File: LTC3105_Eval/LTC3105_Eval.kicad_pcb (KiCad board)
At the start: 2 copper layers, 29.1 x 15.2 mm, 14 parts, among them J1 Conn_01x05_Pin, J2 Conn_01x05_Pin, U1 LTC3105EMS

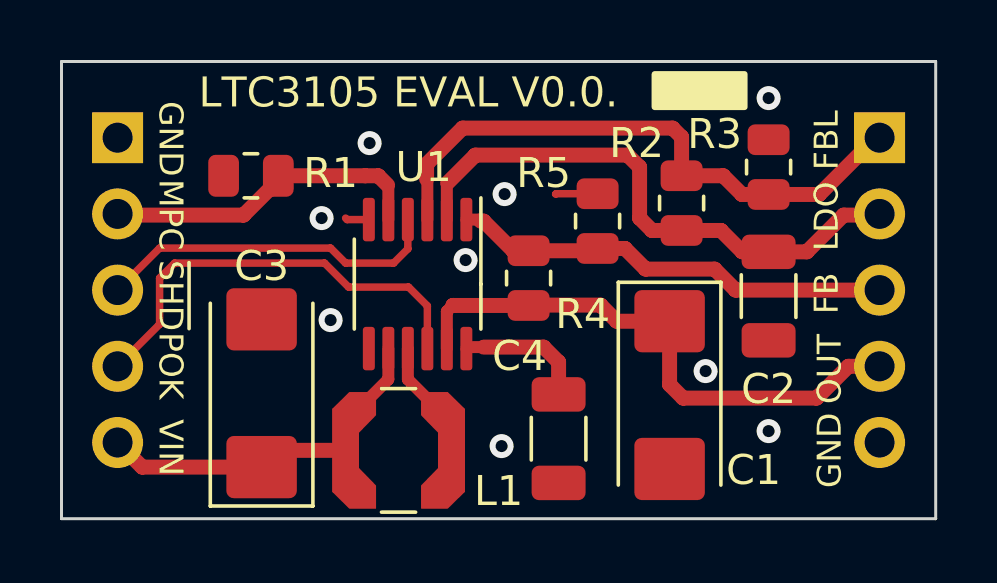
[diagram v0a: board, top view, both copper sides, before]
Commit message: resolved #8, #7, #6 and #5 ; closed #5 and #3
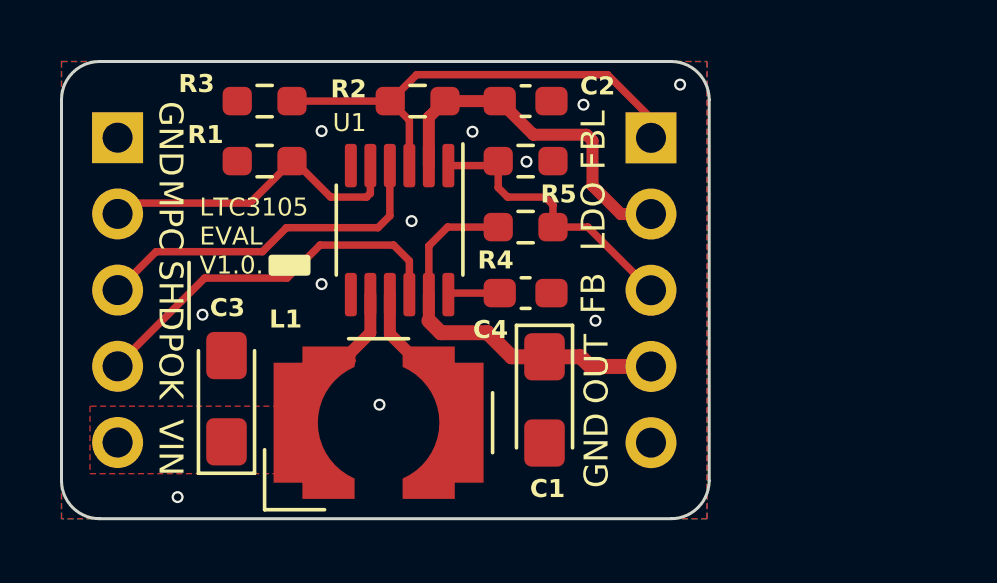
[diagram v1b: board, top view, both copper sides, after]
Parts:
- removed G***: LOGO, QRCODE.preety:LTC3105_Eval_V0_QRCode_5x5
- C1, C3: footprint Capacitor_Tantalum_SMD:CP_EIA-6032-28_Kemet-C -> Capacitor_Tantalum_SMD:CP_EIA-3216-18_Kemet-A_Pad1.58x1.35mm_HandSolder
- C2, C4: footprint Capacitor_SMD:C_1206_3216Metric -> Capacitor_SMD:C_0603_1608Metric_Pad1.08x0.95mm_HandSolder
- L1: value 10uF -> 10uH; footprint Inductor_SMD:L_Coilcraft_LPS4018 -> 021_inductor:L_Coilcraft_MSS5131-XXX_handsolder
- R1, R2, R3, R4, R5: footprint Resistor_SMD:R_0805_2012Metric -> Resistor_SMD:R_0603_1608Metric_Pad0.98x0.95mm_HandSolder
- moved R3 16.9 mm to (131.9, 95.3), turned to 180 degrees
- moved C2 10.4 mm to (140.6, 95.3), turned to 0 degrees
- moved R2 9.43 mm to (137.0, 95.3), turned to 180 degrees
- moved J2 7.62 mm to (144.8, 96.5)
- moved C4 4.98 mm to (140.6, 101.7), turned to 0 degrees
- moved C1 4.17 mm to (141.2, 105.3)
- moved R5 3.12 mm to (140.6, 97.3), turned to 0 degrees
- moved U1 1.90 mm to (136.4, 99.6)
- moved R4 1.70 mm to (140.6, 99.5), turned to 0 degrees
- moved C3 1.18 mm to (130.6, 105.2)
- moved L1 1.14 mm to (135.7, 106.0), turned to 90 degrees
- moved R1 0.67 mm to (131.9, 97.3)
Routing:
- net VIN: track 12.7 -> 2.55 mm
- net LDO_OUT: track 18.9 -> 11.7 mm
- net VOUT: track 18.7 -> 13.1 mm
- net FB: track 14.8 -> 9.55 mm
- net FB_LDO: track 19.9 -> 15.9 mm
- net Net-(U1-AUX): track 4.38 -> 1.73 mm
- net GND: track 2.20 -> 0.00 mm, vias 9 -> 11
- net POWERGOOD: track 14.7 -> 12.8 mm
- net /SW: track 3.99 -> 2.69 mm
- added copper zone on F.Cu, net VIN
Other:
- board size 29.1 x 15.2 mm -> 21.6 x 15.2 mm
- board text added: "LTC3105 EVAL V1.0."
- board text removed: "LTC3105 EVAL V0.0."
